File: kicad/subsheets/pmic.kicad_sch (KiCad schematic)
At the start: 54 parts, among them U2 RK809-5

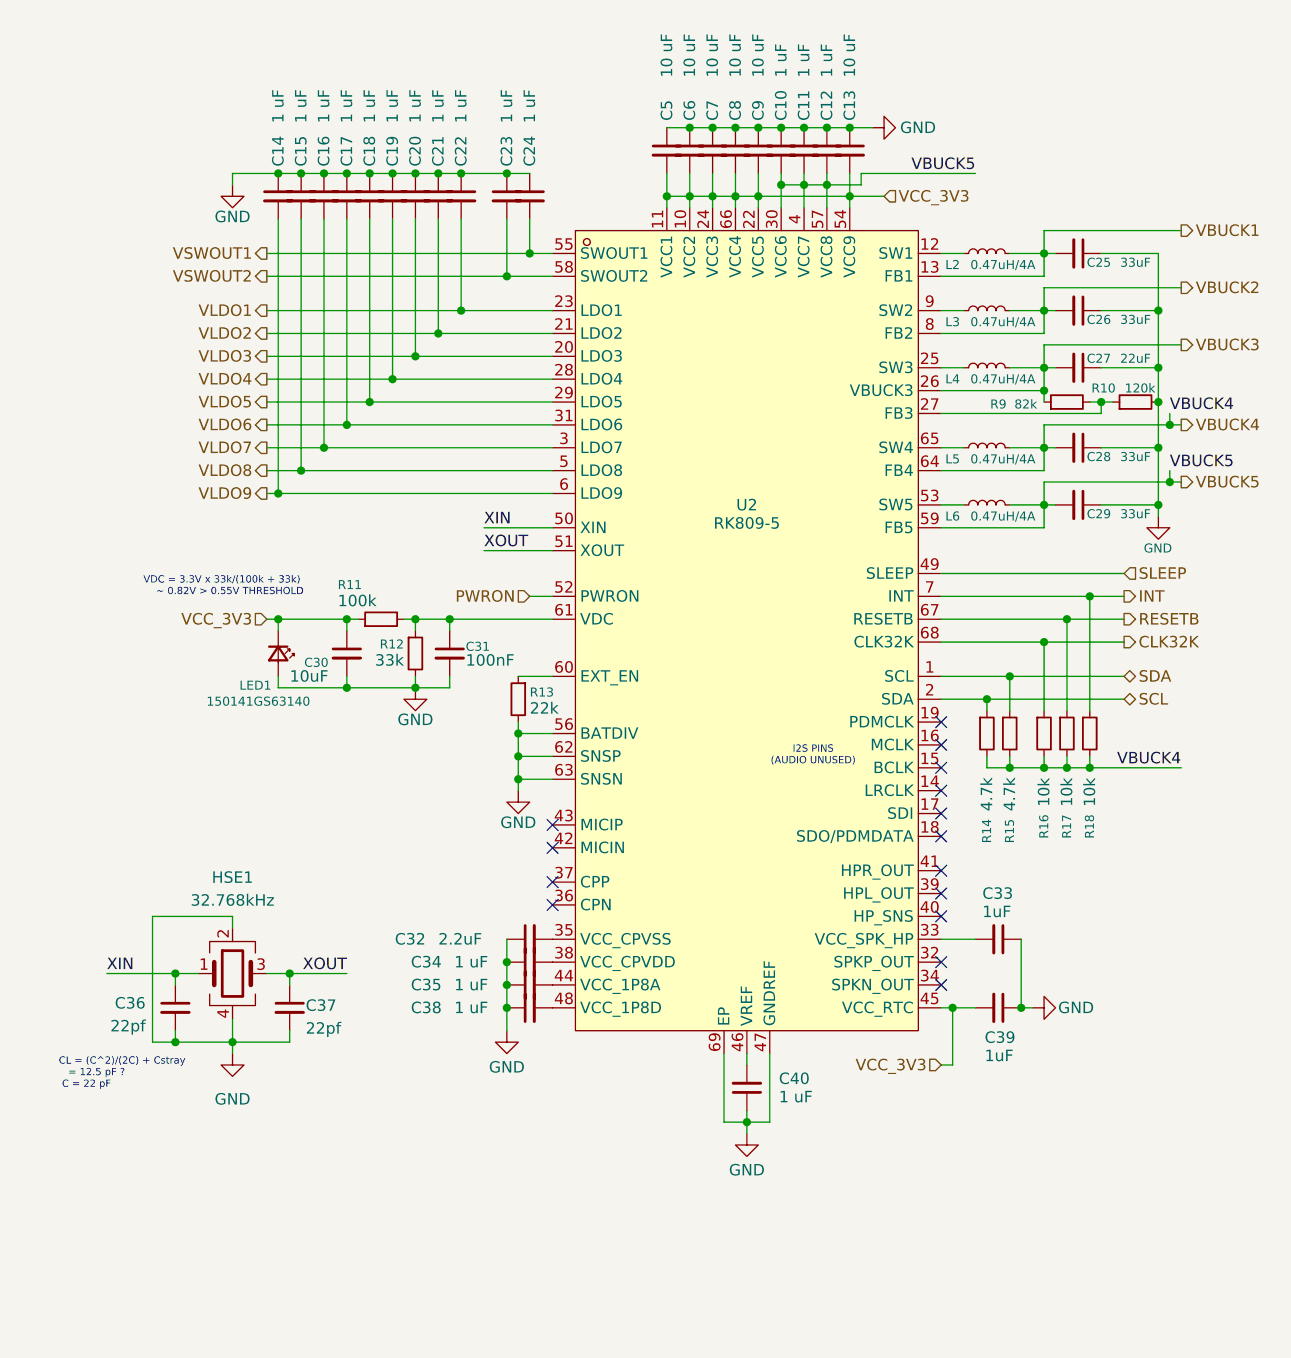
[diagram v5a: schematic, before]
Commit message: Make sure logic levels are correct between ICs
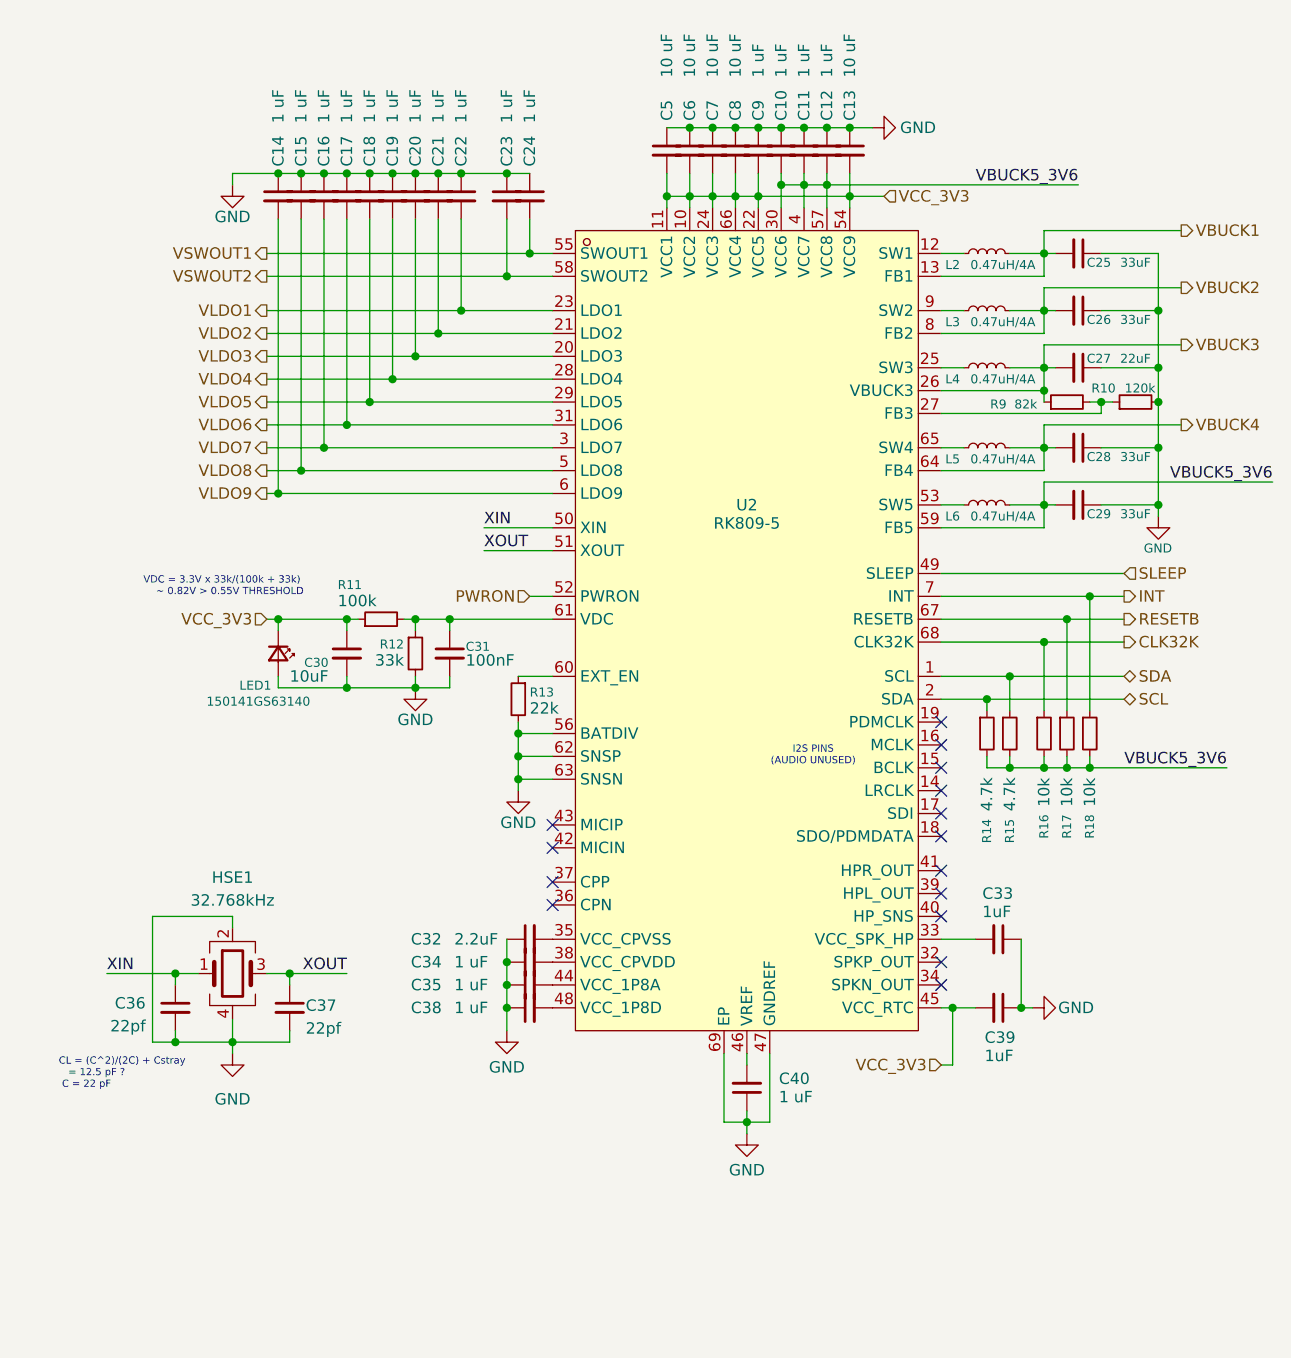
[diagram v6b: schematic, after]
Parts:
- C9: value 10 uF -> 1 uF
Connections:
- net VBUCK4: no longer R14.2, R15.2, R16.2, R17.2, R18.2
- net VBUCK5 renamed VBUCK5_3V6
- net VBUCK5_3V6: now also R14.2, R15.2, R16.2, R17.2, R18.2
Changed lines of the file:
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@@
 	)
 	(junction
-		(at 139.7 59.69)
-		(diameter 0)
-		(color 0 0 0 0)
-	)
-	(junction
 		(at 138.43 68.58)
 		(diameter 0)
@@
 	)
 	(junction
-		(at 139.7 66.04)
-		(diameter 0)
-		(color 0 0 0 0)
-	)
-	(junction
 		(at 91.44 34.29)
 		(diameter 0)
@@
 	(wire
 		(pts
-			(xy 105.41 31.75) (xy 118.11 31.75)
-		)
-		(stroke
-			(width 0)
-			(type default)
-		)
-	)
-	(wire
-		(pts
 			(xy 40.64 88.9) (xy 48.26 88.9)
 		)
@@
 	(wire
 		(pts
-			(xy 139.7 59.69) (xy 140.97 59.69)
+			(xy 125.73 59.69) (xy 140.97 59.69)
 		)
 		(stroke
@@
 	(wire
 		(pts
-			(xy 105.41 33.02) (xy 105.41 31.75)
-		)
-		(stroke
-			(width 0)
-			(type default)
-		)
-	)
-	(wire
-		(pts
 			(xy 125.73 83.82) (xy 125.73 91.44)
 		)
@@
 	(wire
 		(pts
-			(xy 125.73 59.69) (xy 139.7 59.69)
-		)
-		(stroke
-			(width 0)
-			(type default)
-		)
-	)
-	(wire
-		(pts
 			(xy 59.69 81.28) (xy 59.69 82.55)
 		)
@@
 	(wire
 		(pts
-			(xy 139.7 64.77) (xy 139.7 66.04)
-		)
-		(stroke
-			(width 0)
-			(type default)
-		)
-	)
-	(wire
-		(pts
 			(xy 39.37 54.61) (xy 53.34 54.61)
 		)
@@
 	(wire
 		(pts
-			(xy 125.73 66.04) (xy 139.7 66.04)
-		)
-		(stroke
-			(width 0)
-			(type default)
-		)
-	)
-	(wire
-		(pts
 			(xy 55.88 52.07) (xy 71.12 52.07)
 		)
@@
 	(wire
 		(pts
-			(xy 139.7 66.04) (xy 140.97 66.04)
+			(xy 125.73 66.04) (xy 151.13 66.04)
 		)
 		(stroke
@@
 	(wire
 		(pts
-			(xy 130.81 97.79) (xy 140.97 97.79)
+			(xy 130.81 97.79) (xy 146.05 97.79)
 		)
 		(stroke
@@
 	(wire
 		(pts
-			(xy 139.7 58.42) (xy 139.7 59.69)
-		)
-		(stroke
-			(width 0)
-			(type default)
-		)
-	)
-	(wire
-		(pts
 			(xy 48.26 87.63) (xy 48.26 88.9)
 		)
@@
 	(wire
 		(pts
-			(xy 101.6 33.02) (xy 105.41 33.02)
+			(xy 101.6 33.02) (xy 129.54 33.02)
 		)
 		(stroke
@@
 		)
 	)
-	(label "VBUCK5"
-		(at 139.7 64.77 0)
-		(effects
-			(font
-				(size 1.27 1.27)
-			)
-			(justify left bottom)
-		)
-	)
 	(label "XIN"
 		(at 63.5 71.12 0)
@@
 		)
 	)
-	(label "VBUCK4"
-		(at 140.97 97.79 180)
+	(label "VBUCK5_3V6"
+		(at 151.13 66.04 180)
 		(effects
 			(font
@@
 		)
 	)
-	(label "VBUCK4"
-		(at 139.7 58.42 0)
+	(label "VBUCK5_3V6"
+		(at 129.54 33.02 180)
 		(effects
 			(font
 				(size 1.27 1.27)
 			)
-			(justify left bottom)
+			(justify right bottom)
 		)
 	)
-	(label "VBUCK5"
-		(at 118.11 31.75 180)
+	(label "VBUCK5_3V6"
+		(at 146.05 97.79 180)
 		(effects
 			(font
@@
 		)
 	)
-	(hierarchical_label "VBUCK5"
-		(shape output)
-		(at 140.97 66.04 0)
-		(effects
-			(font
-				(size 1.27 1.27)
-			)
-			(justify left)
-		)
-	)
 	(hierarchical_label "VSWOUT1"
 		(shape output)
@@
 			)
 		)
-		(property "Value" "10 uF"
+		(property "Value" "1 uF"
 			(at 93.98 21.082 90)
 			(effects
@@
 		(dnp no)
 		(property "Reference" "C32"
-			(at 53.594 116.84 90)
+			(at 55.372 116.84 90)
 			(effects
 				(font
@@
 		)
 		(property "Value" "2.2uF"
-			(at 58.42 116.84 90)
+			(at 60.198 116.84 90)
 			(effects
 				(font

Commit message: Annotations
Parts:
- added C32: 100nF, symbol Device:C_Small
- renumbered C8 to C10, C9 to C11, C10 to C12, C11 to C13, C12 to C14, C13 to C15, C14 to C16, C15 to C17, C16 to C18, C17 to C19, C18 to C20, C19 to C21, C20 to C22, C21 to C23, C22 to C24, C23 to C25, C24 to C26, C25 to C27, C26 to C28, C27 to C29, C28 to C30, C29 to C31, C30 to C33, C31 to C34, C32 to C35, C33 to C36, C34 to C37, C35 to C38, C36 to C39, C37 to C40, C38 to C41, C39 to C42, C40 to C43, C5 to C7, C6 to C8, C7 to C9, L2 to L3, L3 to L4, L4 to L5, L5 to L6, L6 to L7, R9 to R17, R10 to R18, R11 to R19, R12 to R20, R13 to R21, R14 to R22, R15 to R23, R16 to R24, R17 to R25, R18 to R26, U2 to U3
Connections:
- net GND: now also C32.2; no longer LED1.2 (A)
- net VCC_3V3: no longer C33.1, LED1.1 (K), R19.1
- net PWRON: no longer names the net of U3.52 (PWRON)
- net PWRON: now also C32.1
- new net ENABLE: C33.1, R19.1
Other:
- note added: "Status LED?"
- moved on the sheet: C33, C34, LED1, R19, R20

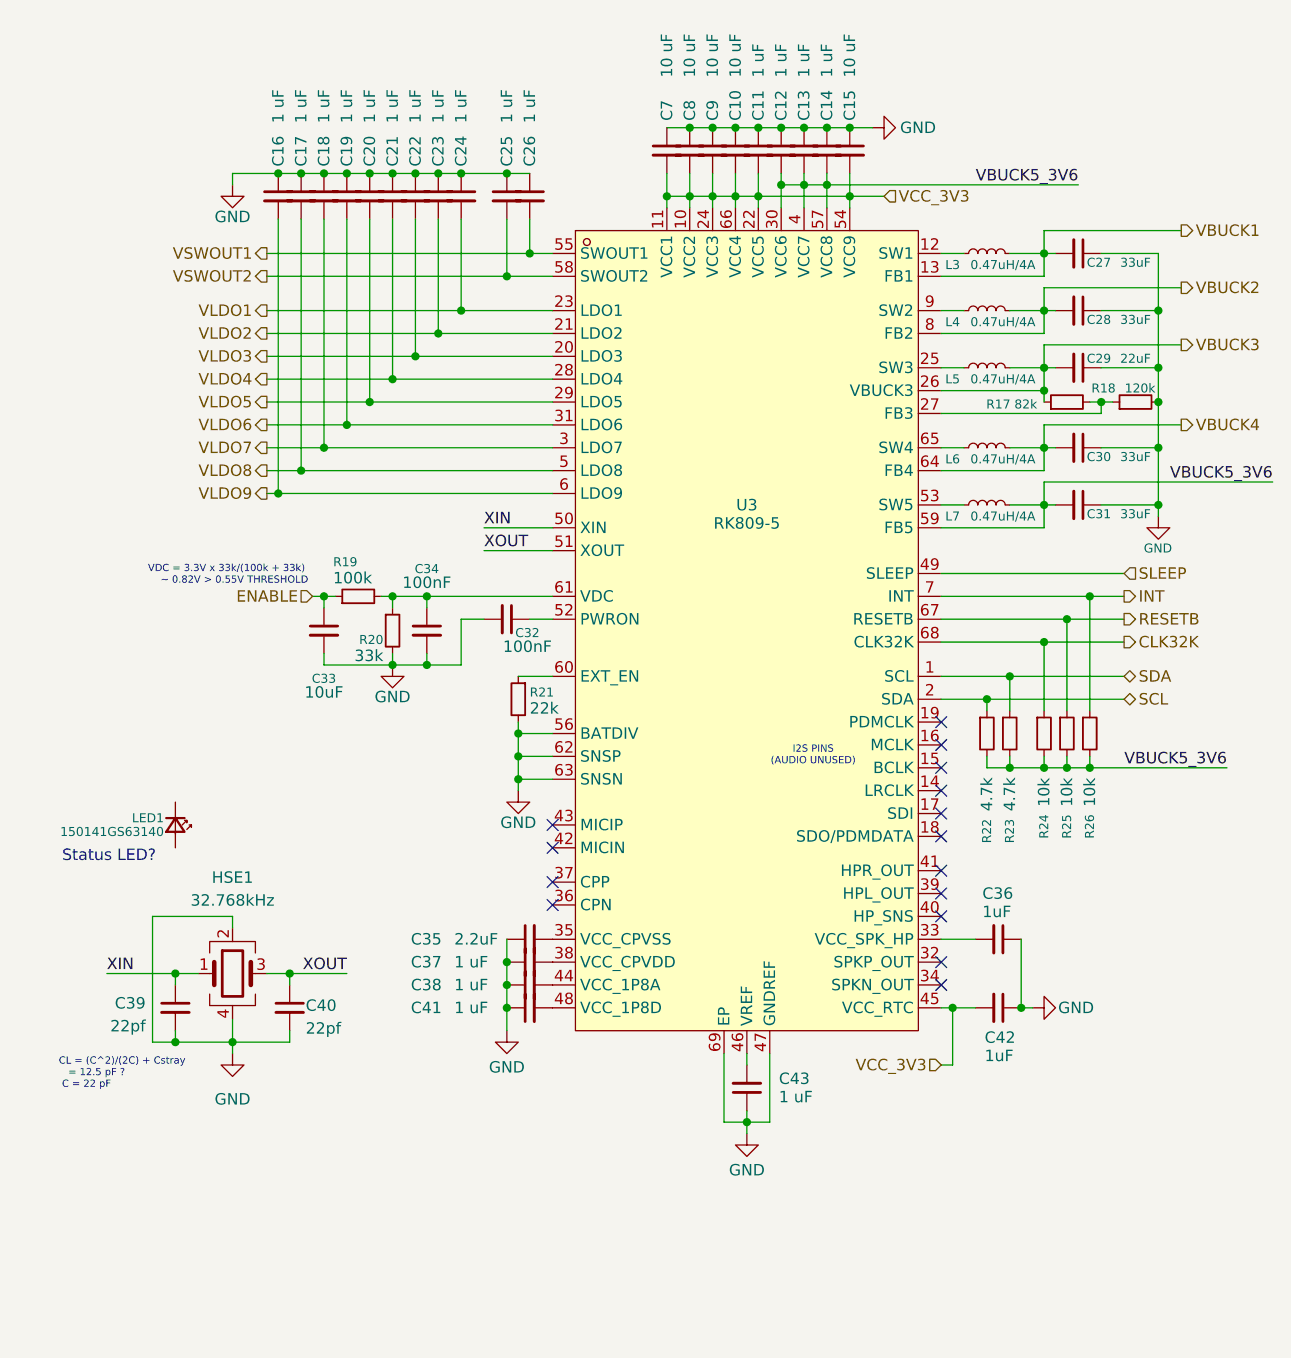
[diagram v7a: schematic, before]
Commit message: Finalized PMIC and added control from STM32
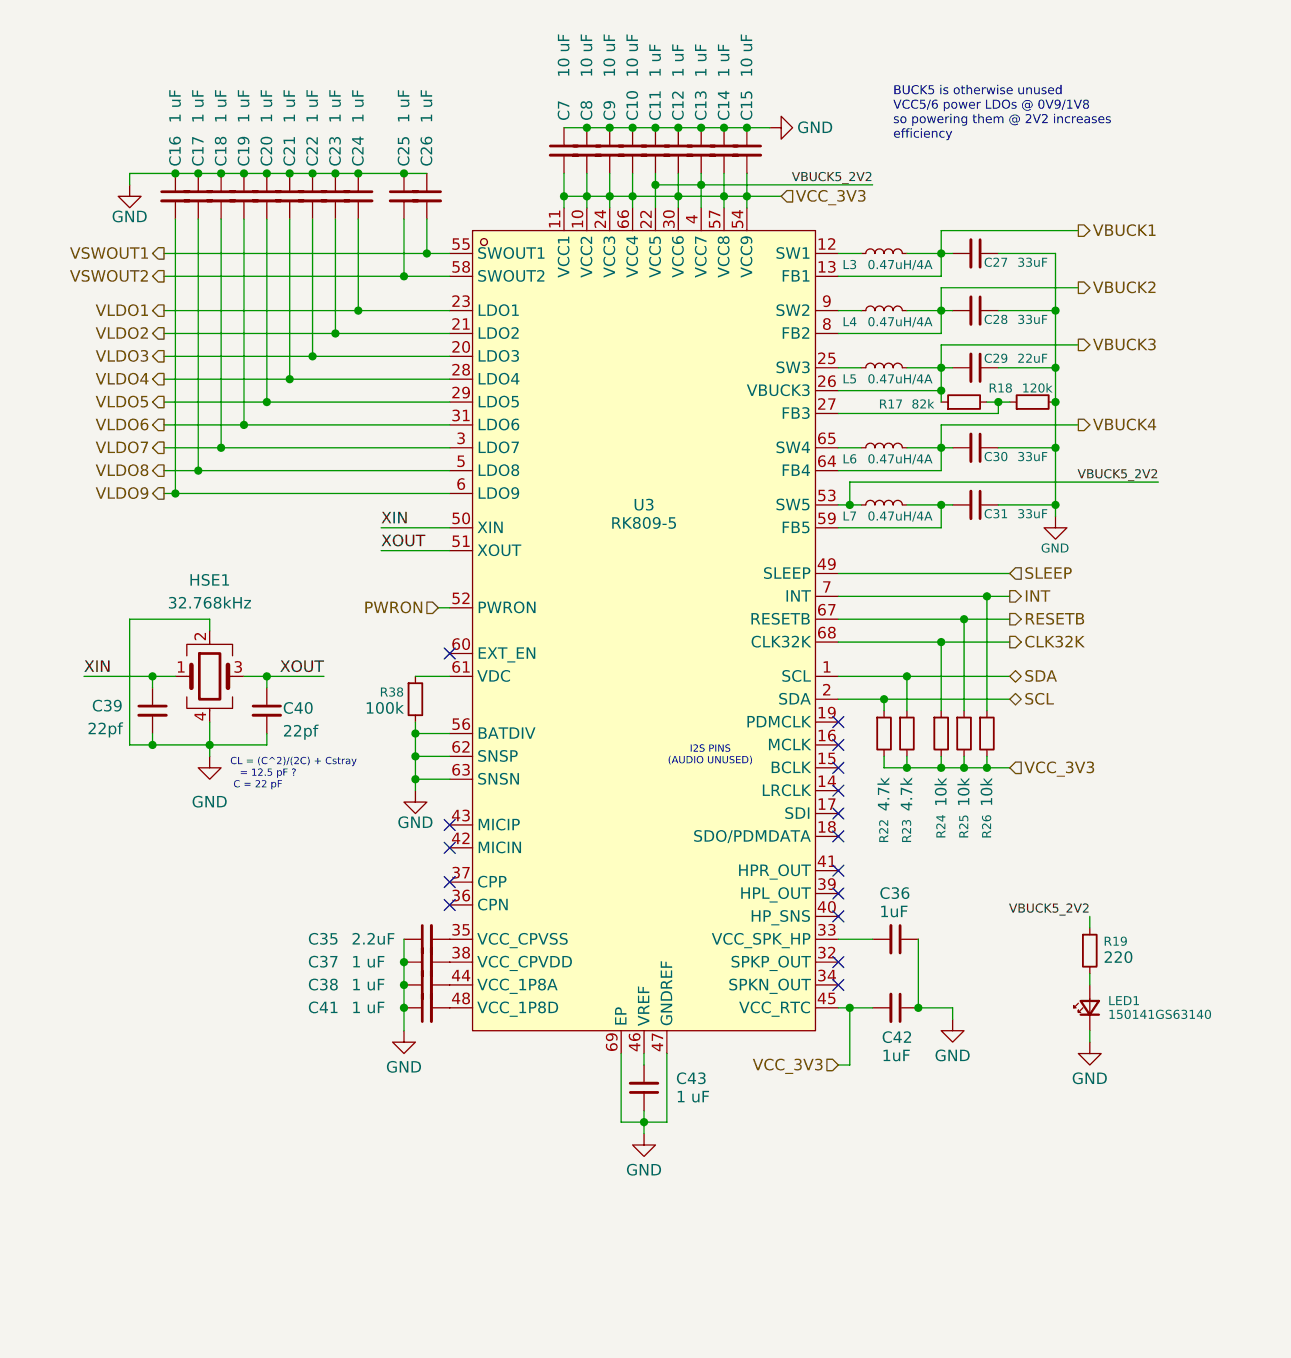
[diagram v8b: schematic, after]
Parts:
- removed C32, C34: 100nF, symbol Device:C_Small
- removed C33: 10uF, symbol Device:C_Small
- removed R20: 33k, symbol Device:R_Small
- removed R21: 22k, symbol Device:R_Small
- added R38: 100k, symbol Device:R_Small
- R19: value 100k -> 220
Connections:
- net ENABLE is gone; now on net VBUCK5_2V2: R19.1
- net GND: now also LED1.1 (K), R38.2
- net VCC_3V3: now also C12.2, C14.2, R22.2, R23.2, R24.2, R25.2, R26.2, U3.30 (VCC6), U3.57 (VCC8); no longer C11.2, U3.22 (VCC5)
- net PWRON: now reaches U3.52 (PWRON)
- net VBUCK5_2V2: now reaches L7.1, U3.53 (SW5)
- net VBUCK5_2V2: now also C11.2, C13.2, U3.22 (VCC5), U3.4 (VCC7)
- net at U3.61 (VDC): now also R38.1; no longer R19.2
- net at LED1.2 (A): now also R19.2
- removed net VBUCK5_3V6: C12.2, C13.2, C14.2, C31.2, L7.2, R22.2, R23.2, R24.2, R25.2, R26.2, U3.30 (VCC6), U3.4 (VCC7), U3.57 (VCC8), U3.59 (FB5)
- new net: C31.2, L7.2, U3.59 (FB5)
- no-connect marks 15 -> 16
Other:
- note added: "BUCK5 is otherwise unused VCC5/6 power LDOs @ 0V9/1V8 so powering them @ 2V2 increases efficiency"
- note removed: "Status LED?"
- note removed: "VDC = 3.3V x 33k/(100k + 33k) ~ 0.82V > 0.55V THRESHOLD"
- moved on the sheet: C10, C11, C12, C13, C14, C15, C16, C17, C18, C19, C20, C21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
